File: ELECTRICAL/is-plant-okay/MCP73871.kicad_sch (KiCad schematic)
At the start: 17 parts, among them U7 MCP73871-2CCI_ML, U8 MIC5365-3.3YMT-TZ

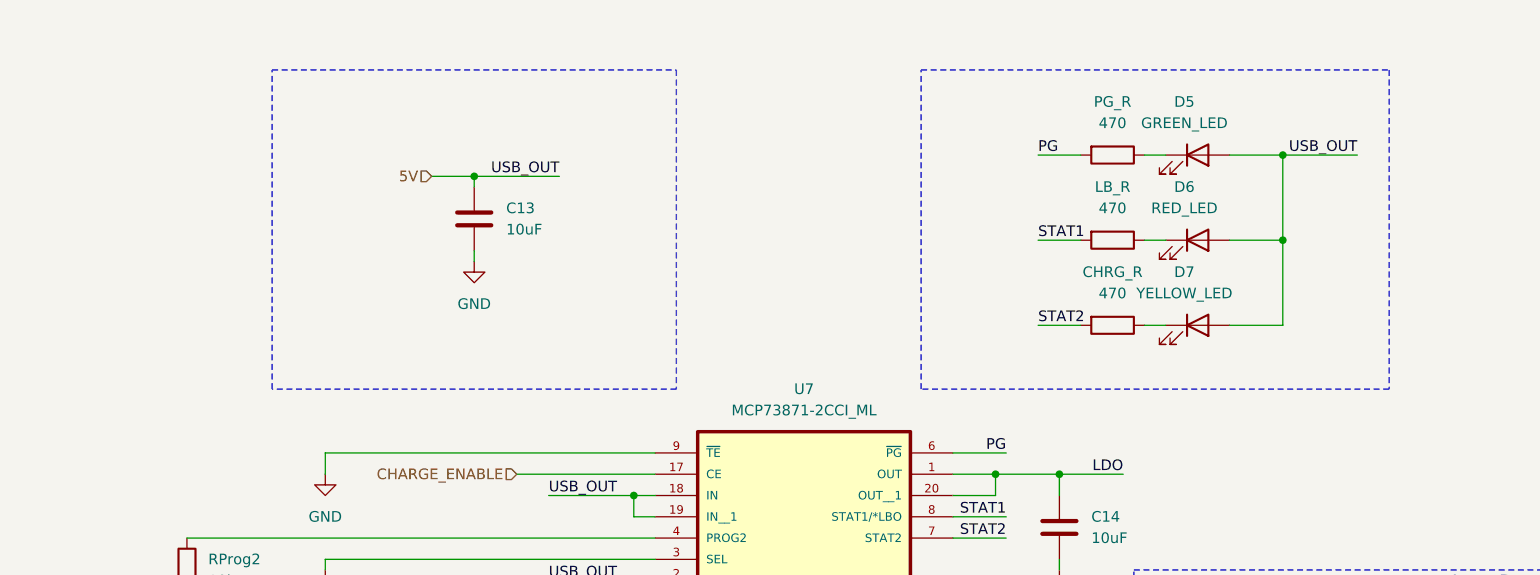
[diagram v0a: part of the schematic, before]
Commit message: feat: add pins for mcu
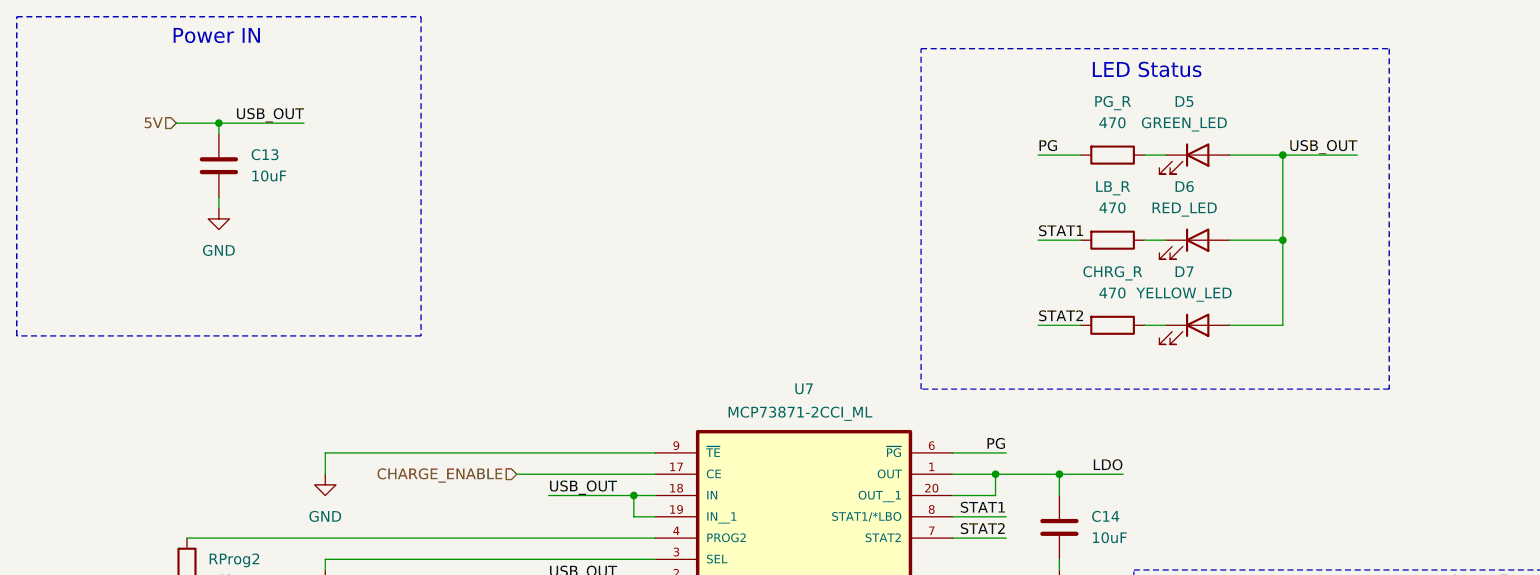
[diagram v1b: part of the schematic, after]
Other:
- note added: "LED Status"
- note added: "Power IN"
- moved on the sheet: C13
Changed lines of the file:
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@@
 	(paper "A4")
 	(rectangle
-		(start 83.82 22.86)
-		(end 132.08 60.96)
+		(start 53.34 16.51)
+		(end 101.6 54.61)
 		(stroke
 			(width 0)
@@
 	)
 	(rectangle
-		(start 161.29 22.86)
+		(start 161.29 20.32)
 		(end 217.17 60.96)
 		(stroke
@@
 		)
 	)
+	(text "LED Status"
+		(exclude_from_sim no)
+		(at 188.214 23.114 0)
+		(effects
+			(font
+				(size 1.778 1.778)
+			)
+		)
+	)
+	(text "Power IN"
+		(exclude_from_sim no)
+		(at 77.216 19.05 0)
+		(effects
+			(font
+				(size 1.778 1.778)
+			)
+		)
+	)
 	(junction
 		(at 125.73 109.22)
@@
 	)
 	(junction
-		(at 107.95 35.56)
+		(at 77.47 29.21)
 		(diameter 0)
 		(color 0 0 0 0)
@@
 	(wire
 		(pts
-			(xy 107.95 35.56) (xy 118.11 35.56)
+			(xy 77.47 29.21) (xy 87.63 29.21)
 		)
 		(stroke
@@
 	(wire
 		(pts
-			(xy 107.95 35.56) (xy 107.95 36.83)
+			(xy 77.47 29.21) (xy 77.47 30.48)
 		)
 		(stroke
@@
 	(wire
 		(pts
-			(xy 107.95 45.72) (xy 107.95 44.45)
+			(xy 77.47 39.37) (xy 77.47 38.1)
 		)
 		(stroke
@@
 	(wire
 		(pts
-			(xy 102.87 35.56) (xy 107.95 35.56)
+			(xy 72.39 29.21) (xy 77.47 29.21)
 		)
 		(stroke
@@
 	)
 	(label "USB_OUT"
-		(at 118.11 35.56 180)
+		(at 87.63 29.21 180)
 		(effects
 			(font
@@
 	(hierarchical_label "5V"
 		(shape input)
-		(at 102.87 35.56 180)
+		(at 72.39 29.21 180)
 		(effects
 			(font
@@
 	(symbol
 		(lib_id "Device:C")
-		(at 107.95 40.64 0)
+		(at 77.47 34.29 0)
 		(unit 1)
 		(exclude_from_sim no)
@@
 		(fields_autoplaced yes)
 		(property "Reference" "C13"
-			(at 111.76 39.3699 0)
+			(at 81.28 33.0199 0)
 			(effects
 				(font
@@
 		)
 		(property "Value" "10uF"
-			(at 111.76 41.9099 0)
+			(at 81.28 35.5599 0)
 			(effects
 				(font
@@
 		)
 		(property "Footprint" ""
-			(at 108.9152 44.45 0)
+			(at 78.4352 38.1 0)
 			(effects
 				(font
@@
 		)
 		(property "Datasheet" "~"
-			(at 107.95 40.64 0)
+			(at 77.47 34.29 0)
 			(effects
 				(font
@@
 		)
 		(property "Description" "Unpolarized capacitor"
-			(at 107.95 40.64 0)
+			(at 77.47 34.29 0)
 			(effects
 				(font
@@
 		(on_board yes)
 		(dnp no)
-		(fields_autoplaced yes)
 		(property "Reference" "U7"
 			(at 147.32 60.96 0)
@@
 		)
 		(property "Value" "MCP73871-2CCI_ML"
-			(at 147.32 63.5 0)
+			(at 146.812 63.754 0)
 			(effects
 				(font
@@
 	(symbol
 		(lib_id "power:GND")
-		(at 107.95 45.72 0)
+		(at 77.47 39.37 0)
 		(unit 1)
 		(exclude_from_sim no)
@@
 		(fields_autoplaced yes)
 		(property "Reference" "#PWR043"
-			(at 107.95 52.07 0)
+			(at 77.47 45.72 0)
 			(effects
 				(font
@@
 		)
 		(property "Value" "GND"
-			(at 107.95 50.8 0)
+			(at 77.47 44.45 0)
 			(effects
 				(font
@@
 		)
 		(property "Footprint" ""
-			(at 107.95 45.72 0)
+			(at 77.47 39.37 0)
 			(effects
 				(font
@@
 		)
 		(property "Datasheet" ""
-			(at 107.95 45.72 0)
+			(at 77.47 39.37 0)
 			(effects
 				(font
@@
 		)
 		(property "Description" "Power symbol creates a global label with name \"GND\" , ground"
-			(at 107.95 45.72 0)
-			(effects
-				(font
+			(at 77.47 39.37 0)
+			(effects
+				(font

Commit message: feat: finished schematics
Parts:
- added BT1: 254TR_-, is-plant-okay-foot:BAT_254TR, symbol is-plant-okay-lib:254TR
- added RProg4: 0, symbol Device:R
- added TP9: LDO_3.3V_TP, TestPoint:TestPoint_Keystone_5000-5004_Miniature, symbol Connector:TestPoint
- BT3: value 254TR -> 254TR_+
- RProg2: value 10k -> 1k; now not fitted; now left out of the parts list
- renumbered CHRG_R to CHRG_R1, LB_R to LB_R1, PG_R to PG_R1
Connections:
- net CHARGE_ENABLE is gone; now on net 5V: U7.17 (CE)
- net 5V: now also RProg2.2
- net GND: now also BT1.P1, BT1.P2, RProg4.1, TP9.1; no longer RProg2.2
- net at RProg2.1, U7.4 (PROG2): now also RProg4.2

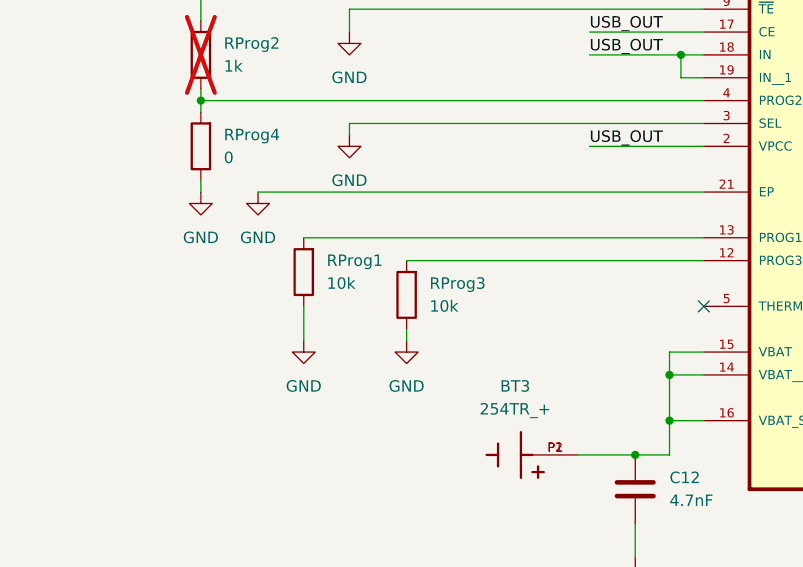
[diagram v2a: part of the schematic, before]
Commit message: feat: add resistor footprint
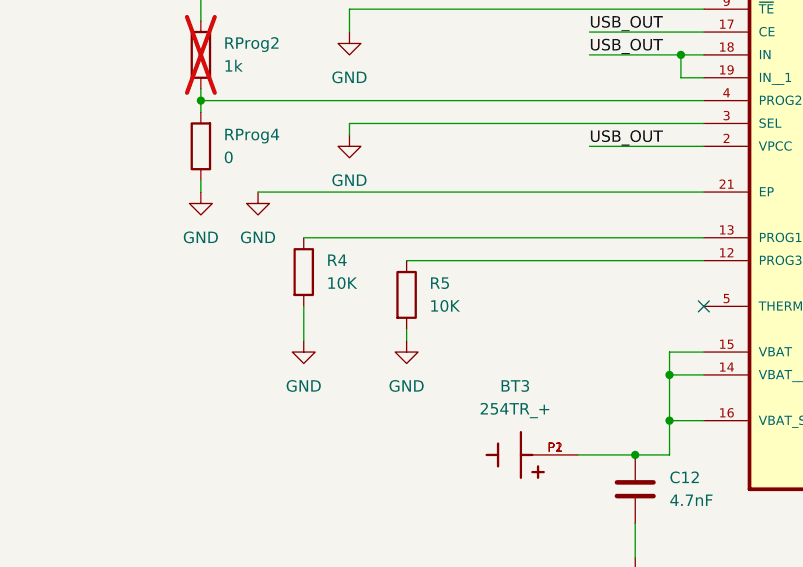
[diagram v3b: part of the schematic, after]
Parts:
- removed RProg1, RProg3: 10k, symbol Device:R
- added R4, R5: 10K, is-plant-okay-foot:RC0805FR-7W10KL, symbol Device:R
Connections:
- net GND: now also R4.2, R5.2
- net at U7.12 (PROG3): now also R5.1
- net at U7.13 (PROG1): now also R4.1
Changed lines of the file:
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@@
+	(symbol
+		(lib_id "Device:R")
+		(at 96.52 100.33 0)
+		(unit 1)
+		(exclude_from_sim no)
+		(in_bom yes)
+		(on_board yes)
+		(dnp no)
+		(fields_autoplaced yes)
+		(property "Reference" "R5"
+			(at 99.06 99.0599 0)
+			(effects
+				(font
+					(size 1.27 1.27)
+				)
+				(justify left)
+			)
+		)
+		(property "Value" "10K"
+			(at 99.06 101.5999 0)
+			(effects
+				(font
+					(size 1.27 1.27)
+				)
+				(justify left)
+			)
+		)
+		(property "Footprint" "is-plant-okay-foot:RC0805FR-7W10KL"
+			(at 94.742 100.33 90)
+			(effects
+				(font
+					(size 1.27 1.27)
+				)
+				(hide yes)
+			)
+		)
+		(property "Datasheet" "~https://www.yageogroup.com/content/datasheet/asset/file/PYU-RC_GROUP_51_ROHS_L"
+			(at 96.52 100.33 0)
+			(effects
+				(font
+					(size 1.27 1.27)
+				)
+				(hide yes)
+			)
+		)
+		(property "Description" "RES 10K OHM 1% 1/4W 0805"
+			(at 96.52 100.33 0)
+			(effects
+				(font
+					(size 1.27 1.27)
+				)
+				(hide yes)
+			)
+		)
+		(property "MFG PART #" "RC0805FR-7W10KL"
+			(at 96.52 100.33 0)
+			(effects
+				(font
+					(size 1.27 1.27)
+				)
+				(hide yes)
+			)
+		)
+		(property "TYPE" "SMD"
+			(at 96.52 100.33 0)
+			(effects
+				(font
+					(size 1.27 1.27)
+				)
+				(hide yes)
+			)
+		)
+		(property "PACKAGE" "0805"
+			(at 96.52 100.33 0)
+			(effects
+				(font
+					(size 1.27 1.27)
+				)
+				(hide yes)
+			)
+		)
+		(pin "1"
+		)
+		(pin "2"
+		)
+		(instances
+			(project "is-plant-okay"
+				(path "/ac51c2f9-77a4-4b89-b63f-6e0ba02b1e45/8bf9bca6-f39d-47ed-80ea-99ec258c6971"
+					(reference "R5")
+					(unit 1)
+				)
+			)
+		)
+	)
 	(symbol
 		(lib_id "Device:R")
@@
 	)
 	(symbol
-		(lib_id "Device:R")
-		(at 85.09 97.79 180)
-		(unit 1)
-		(exclude_from_sim no)
-		(in_bom yes)
-		(on_board yes)
-		(dnp no)
-		(fields_autoplaced yes)
-		(property "Reference" "RProg1"
-			(at 87.63 96.5199 0)
-			(effects
-				(font
-					(size 1.27 1.27)
-				)
-				(justify right)
-			)
-		)
-		(property "Value" "10k"
-			(at 87.63 99.0599 0)
-			(effects
-				(font
-					(size 1.27 1.27)
-				)
-				(justify right)
-			)
-		)
-		(property "Footprint" ""
-			(at 86.868 97.79 90)
-			(effects
-				(font
-					(size 1.27 1.27)
-				)
-				(hide yes)
-			)
-		)
-		(property "Datasheet" "~"
-			(at 85.09 97.79 0)
-			(effects
-				(font
-					(size 1.27 1.27)
-				)
-				(hide yes)
-			)
-		)
-		(property "Description" "Resistor"
-			(at 85.09 97.79 0)
-			(effects
-				(font
-					(size 1.27 1.27)
-				)
-				(hide yes)
-			)
-		)
-		(pin "1"
-		)
-		(pin "2"
-		)
-		(instances
-			(project ""
-				(path "/ac51c2f9-77a4-4b89-b63f-6e0ba02b1e45/8bf9bca6-f39d-47ed-80ea-99ec258c6971"
-					(reference "RProg1")
-					(unit 1)
-				)
-			)
-		)
-	)
-	(symbol
 		(lib_id "Device:C")
 		(at 177.8 77.47 0)
@@
 	)
 	(symbol
-		(lib_id "Device:R")
-		(at 96.52 100.33 180)
-		(unit 1)
-		(exclude_from_sim no)
-		(in_bom yes)
-		(on_board yes)
-		(dnp no)
-		(fields_autoplaced yes)
-		(property "Reference" "RProg3"
-			(at 99.06 99.0599 0)
-			(effects
-				(font
-					(size 1.27 1.27)
-				)
-				(justify right)
-			)
-		)
-		(property "Value" "10k"
-			(at 99.06 101.5999 0)
-			(effects
-				(font
-					(size 1.27 1.27)
-				)
-				(justify right)
-			)
-		)
-		(property "Footprint" ""
-			(at 98.298 100.33 90)
-			(effects
-				(font
-					(size 1.27 1.27)
-				)
-				(hide yes)
-			)
-		)
-		(property "Datasheet" "~"
-			(at 96.52 100.33 0)
-			(effects
-				(font
-					(size 1.27 1.27)
-				)
-				(hide yes)
-			)
-		)
-		(property "Description" "Resistor"
-			(at 96.52 100.33 0)
-			(effects
-				(font
-					(size 1.27 1.27)
-				)
-				(hide yes)
-			)
-		)
-		(pin "1"
-		)
-		(pin "2"
-		)
-		(instances
-			(project "is-plant-okay"
-				(path "/ac51c2f9-77a4-4b89-b63f-6e0ba02b1e45/8bf9bca6-f39d-47ed-80ea-99ec258c6971"
-					(reference "RProg3")
-					(unit 1)
-				)
-			)
-		)
-	)
-	(symbol
 		(lib_id "Device:C")
 		(at 121.92 121.92 0)
@@
 					(unit 1)
 				)
+			)
+		)
+	)
+	(symbol
+		(lib_id "Device:R")
+		(at 85.09 97.79 0)
+		(unit 1)
+		(exclude_from_sim no)
+		(in_bom yes)
+		(on_board yes)
+		(dnp no)
+		(fields_autoplaced yes)
+		(property "Reference" "R4"
+			(at 87.63 96.5199 0)
+			(effects
+				(font
+					(size 1.27 1.27)
+				)
+				(justify left)
+			)
+		)
+		(property "Value" "10K"
+			(at 87.63 99.0599 0)
+			(effects
+				(font
+					(size 1.27 1.27)
+				)
+				(justify left)
+			)
+		)
+		(property "Footprint" "is-plant-okay-foot:RC0805FR-7W10KL"
+			(at 83.312 97.79 90)
+			(effects
+				(font
+					(size 1.27 1.27)
+				)
+				(hide yes)
+			)
+		)
+		(property "Datasheet" "~https://www.yageogroup.com/content/datasheet/asset/file/PYU-RC_GROUP_51_ROHS_L"
+			(at 85.09 97.79 0)
+			(effects
+				(font
+					(size 1.27 1.27)
+				)
+				(hide yes)
+			)
+		)
+		(property "Description" "RES 10K OHM 1% 1/4W 0805"
+			(at 85.09 97.79 0)
+			(effects
+				(font
+					(size 1.27 1.27)
+				)
+				(hide yes)
+			)
+		)
+		(property "MFG PART #" "RC0805FR-7W10KL"
+			(at 85.09 97.79 0)
+			(effects
+				(font
+					(size 1.27 1.27)
+				)
+				(hide yes)
+			)
+		)
+		(property "TYPE" "SMD"
+			(at 85.09 97.79 0)
+			(effects
+				(font
+					(size 1.27 1.27)
+				)
+				(hide yes)
+			)
+		)
+		(property "PACKAGE" "0805"
+			(at 85.09 97.79 0)
+			(effects
+				(font
+					(size 1.27 1.27)
+				)
+				(hide yes)
+			)
+		)
+		(pin "1"
+		)
+		(pin "2"
+		)
+		(instances
+			(project "is-plant-okay"
+				(path "/ac51c2f9-77a4-4b89-b63f-6e0ba02b1e45/8bf9bca6-f39d-47ed-80ea-99ec258c6971"
+					(reference "R4")
+					(unit 1)
+				)

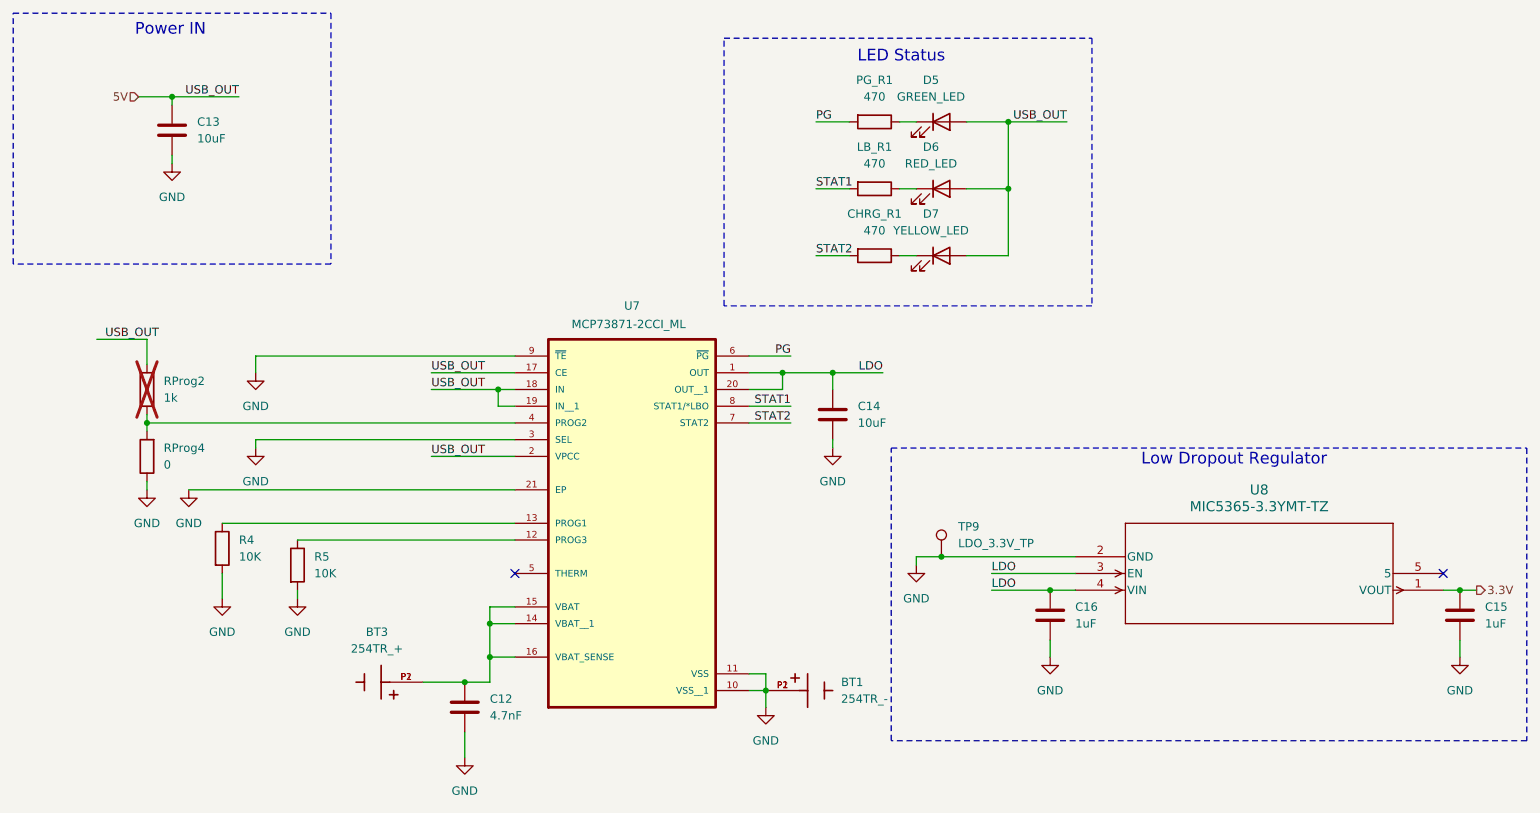
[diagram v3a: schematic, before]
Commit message: feat: add remaining resistor, capacitor footprints
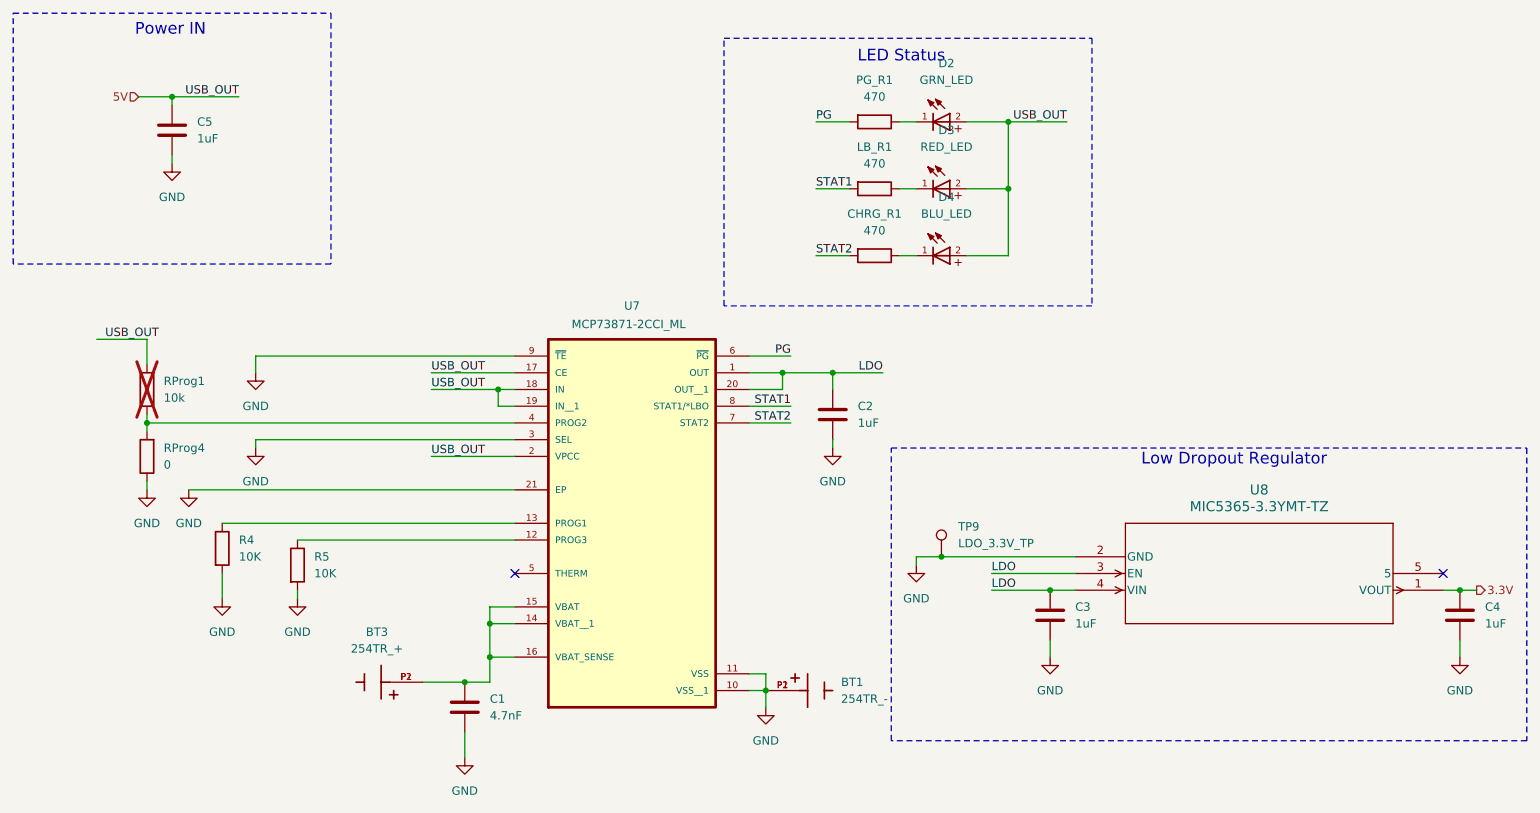
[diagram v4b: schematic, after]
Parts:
- removed C12: 4.7nF, symbol Device:C
- removed C13, C14: 10uF, symbol Device:C
- removed C15, C16: 1uF, symbol Device:C
- removed D5: GREEN_LED, symbol Device:LED
- removed D6: RED_LED, symbol Device:LED
- removed D7: YELLOW_LED, symbol Device:LED
- removed RProg2: 1k, symbol Device:R
- added C1: 4.7nF, is-plant-okay-foot:CAPC1005X55N, symbol Device:C
- added C2, C3, C4, C5: 1uF, is-plant-okay-foot:CAPC3216X180N, symbol Device:C
- added D2: GRN_LED, is-plant-okay-foot:150120GS75000, symbol is-plant-okay-lib:WL-SMCW_1206
- added D3: RED_LED, is-plant-okay-foot:150120GS75000, symbol is-plant-okay-lib:WL-SMCW_1206
- added D4: BLU_LED, is-plant-okay-foot:150120GS75000, symbol is-plant-okay-lib:WL-SMCW_1206
- added RProg1: 10k, is-plant-okay-foot:RES_ZOR25_6P3X2P3_YAG, symbol Device:R
- CHRG_R1, LB_R1, PG_R1: footprint (none) -> is-plant-okay-foot:RESC2012X65N; PACKAGE (none) -> 0805; TYPE (none) -> SMD
- RProg4: footprint (none) -> is-plant-okay-foot:RES_ZOR25_6P3X2P3_YAG; MFG PART # (none) -> ZOR-25-B-52-0R; TYPE (none) -> thru-hole
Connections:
- net 3.3V: now also C4.1
- net 5V: now also C5.1, D2.2, D3.2, D4.2, RProg1.2
- net GND: now also C1.2, C2.2, C3.2, C4.2, C5.2
- net LDO: now also C2.1, C3.1
- net at BT3.P1, BT3.P2, U7.14 (VBAT__1)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: now also C1.1
- net at RProg4.2, U7.4 (PROG2): now also RProg1.1
- net at CHRG_R1.1: now also D4.1
- net at PG_R1.1: now also D2.1
- net at LB_R1.1: now also D3.1
